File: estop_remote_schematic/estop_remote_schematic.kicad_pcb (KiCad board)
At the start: 2 copper layers, 13 parts

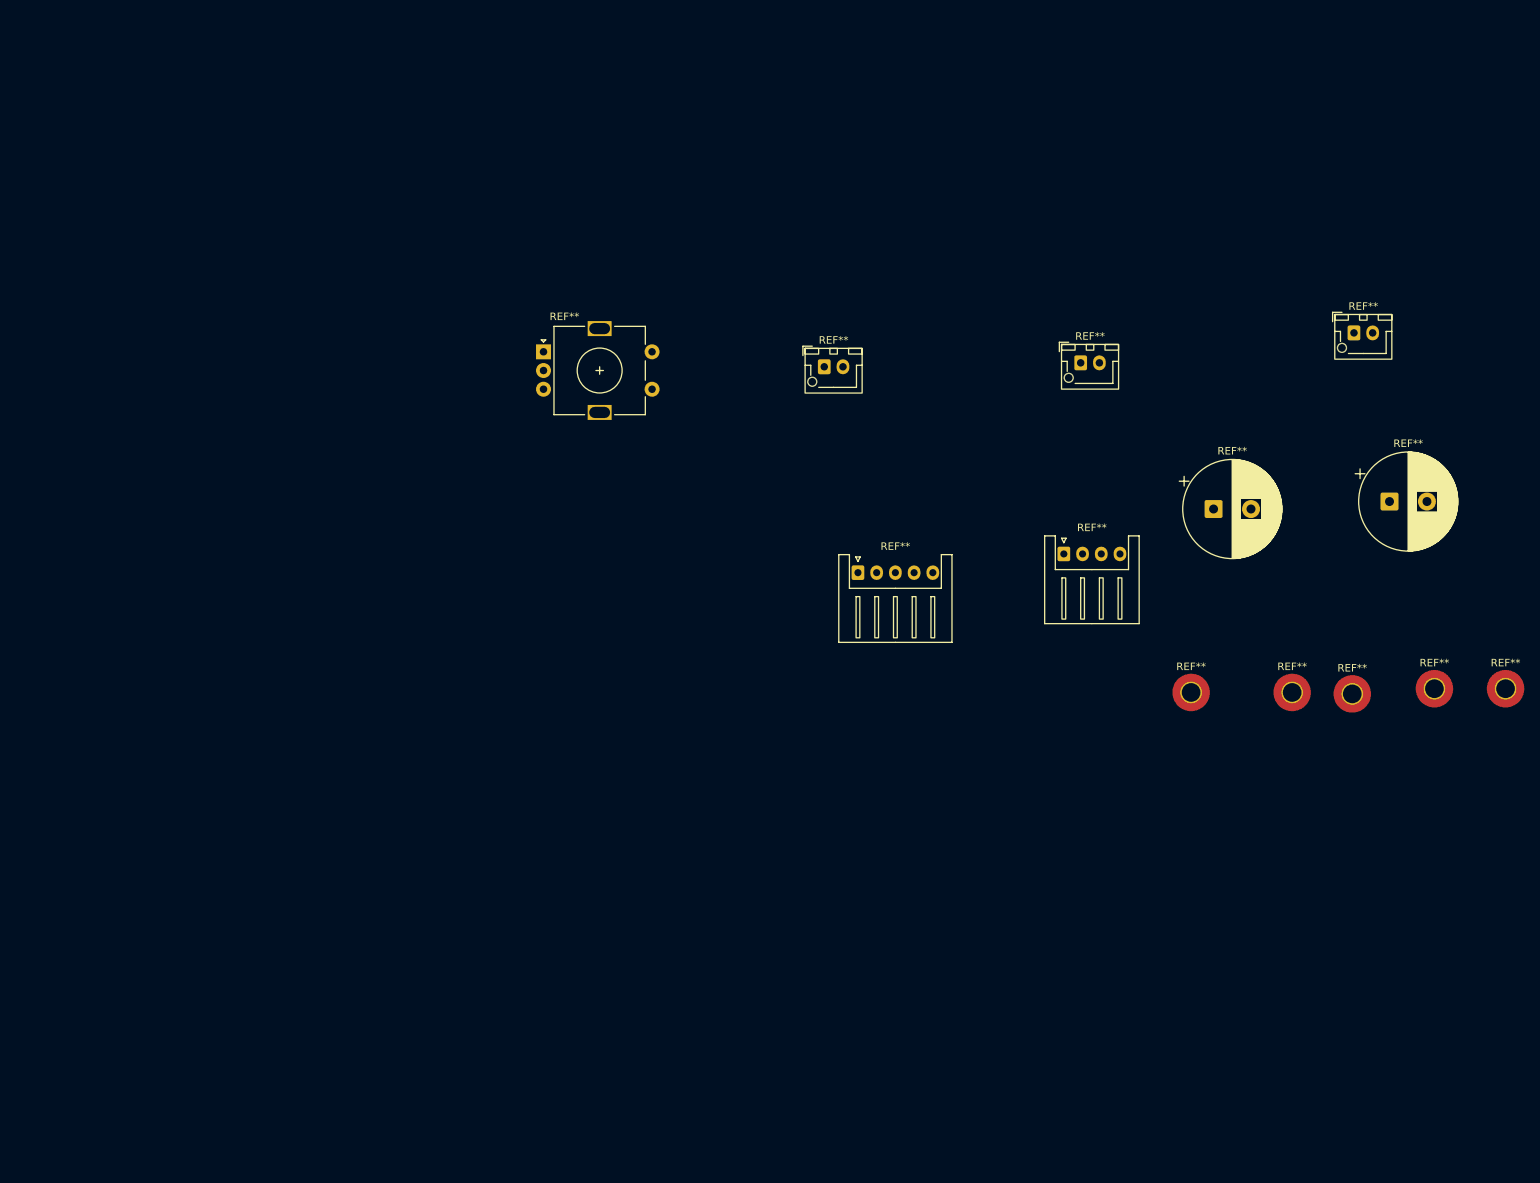
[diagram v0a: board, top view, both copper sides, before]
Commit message: updated footprints, cleaned up global labels and updated preliminary PCB to be more accurate
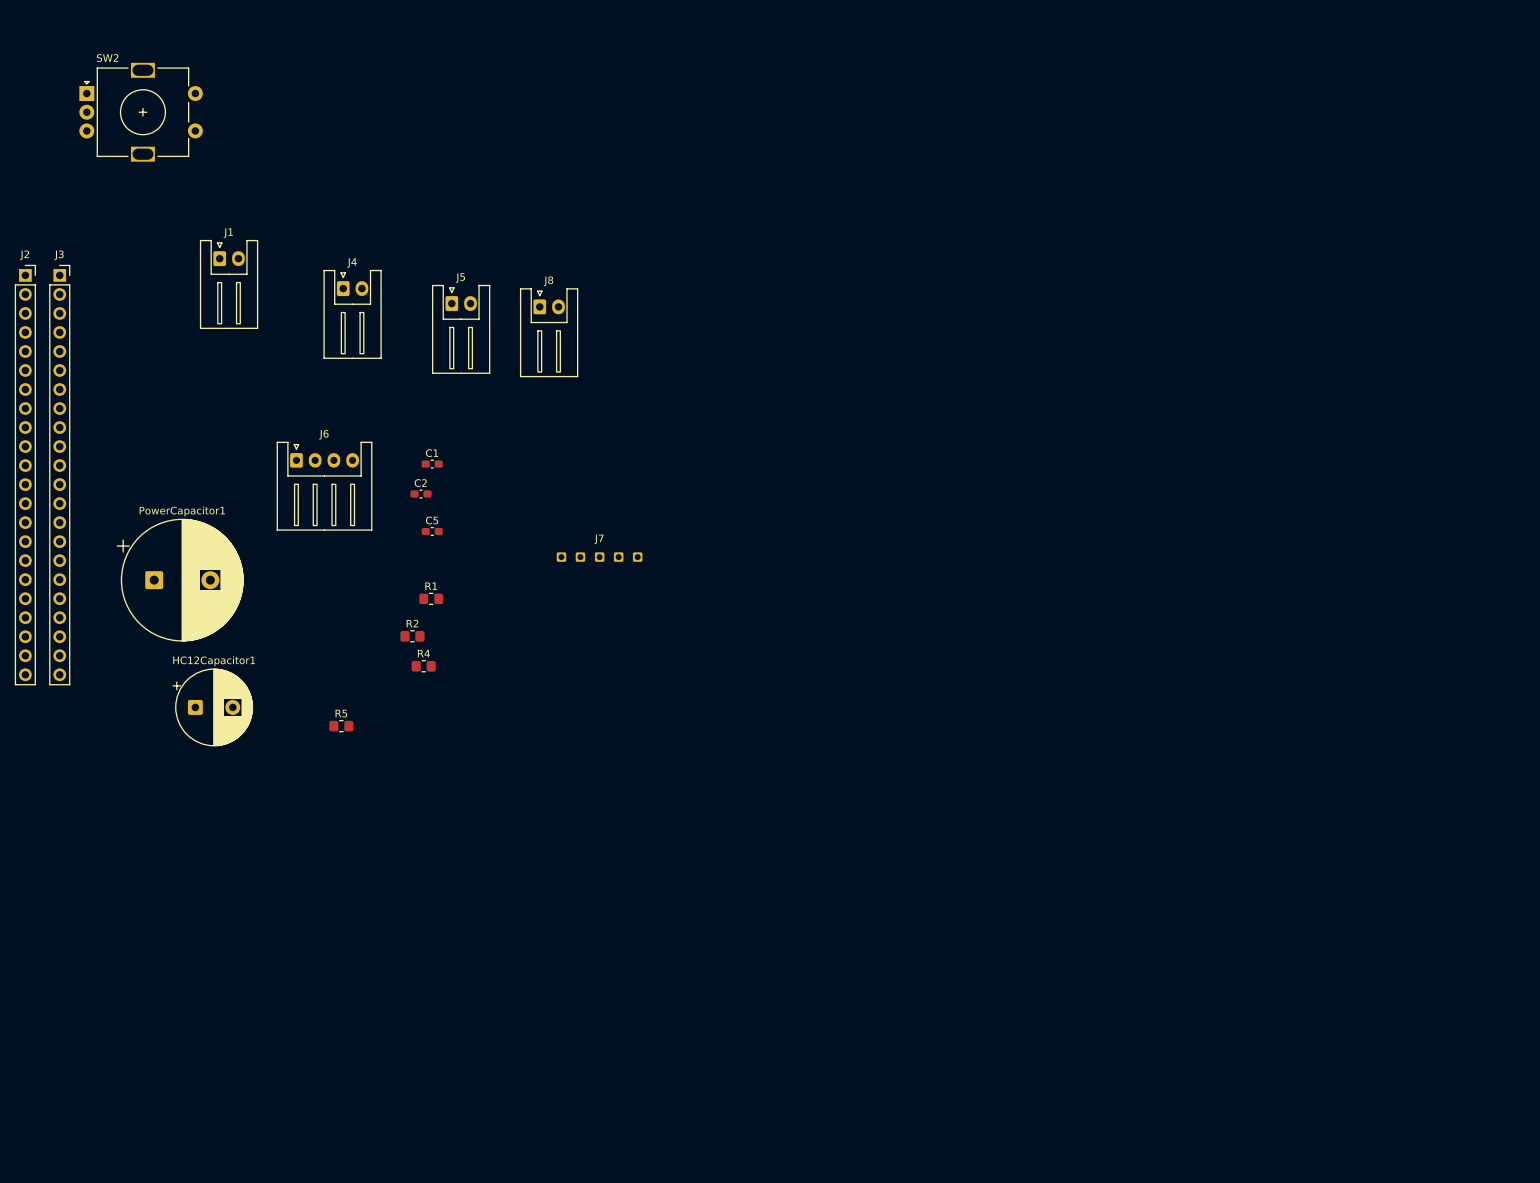
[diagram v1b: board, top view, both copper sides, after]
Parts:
- removed REF**: JST_XH_S5B-XH-A_1x05_P2.50mm_Horizontal, Connector_JST:JST_XH_S5B-XH-A_1x05_P2.50mm_Horizontal
- removed REF**: JST_XH_S4B-XH-A_1x04_P2.50mm_Horizontal, Connector_JST:JST_XH_S4B-XH-A_1x04_P2.50mm_Horizontal
- removed REF** (x3): JST_XH_B2B-XH-AM_1x02_P2.50mm_Vertical, Connector_JST:JST_XH_B2B-XH-AM_1x02_P2.50mm_Vertical
- removed REF** (x5): MountingHole_2.5mm_Pad_TopOnly, MountingHole:MountingHole_2.5mm_Pad_TopOnly
- removed REF**: RotaryEncoder_Alps_EC11E-Switch_Vertical_H20mm, Rotary_Encoder:RotaryEncoder_Alps_EC11E-Switch_Vertical_H20mm
- removed REF** (x2): CP_Radial_D13.0mm_P5.00mm, Capacitor_THT:CP_Radial_D13.0mm_P5.00mm
- added C1: 0.1uF, Capacitor_SMD:C_0603_1608Metric_Pad1.08x0.95mm_HandSolder, F.Cu at (113.1, 88.0)
- added C2: 0.1uF, Capacitor_SMD:C_0603_1608Metric_Pad1.08x0.95mm_HandSolder, F.Cu at (111.6, 92.0)
- added C5: 0.1uF, Capacitor_SMD:C_0603_1608Metric_Pad1.08x0.95mm_HandSolder, F.Cu at (113.1, 97.0)
- added HC12Capacitor1: 220uF, Capacitor_THT:CP_Radial_D10.0mm_P5.00mm, F.Cu at (81.5, 120.5)
- added J1: Power Switch, Connector_JST:JST_XH_S2B-XH-A_1x02_P2.50mm_Horizontal, F.Cu at (84.8, 60.6)
- added J2: ESP32 Pins 1-22, Connector_PinSocket_2.54mm:PinSocket_1x22_P2.54mm_Vertical, F.Cu at (58.8, 62.8)
- added J3: ESP32 Pins 23-44, Connector_PinSocket_2.54mm:PinSocket_1x22_P2.54mm_Vertical, F.Cu at (63.4, 62.8)
- added J4: Battery Connector, Connector_JST:JST_XH_S2B-XH-A_1x02_P2.50mm_Horizontal, F.Cu at (101.2, 64.6)
- added J5: EStop Button, Connector_JST:JST_XH_S2B-XH-A_1x02_P2.50mm_Horizontal, F.Cu at (115.8, 66.6)
- added J6: OLed Screen Pins, Connector_JST:JST_XH_S4B-XH-A_1x04_P2.50mm_Horizontal, F.Cu at (95.0, 87.5)
- added J7: HC12 Connections, holes:2.54mm-5-holes, F.Cu at (135.5, 100.5)
- added J8: Reset Button, Connector_JST:JST_XH_S2B-XH-A_1x02_P2.50mm_Horizontal, F.Cu at (127.5, 67.0)
- added PowerCapacitor1: 2200uF, Capacitor_THT:CP_Radial_D16.0mm_P7.50mm, F.Cu at (76.0, 103.5)
- added R1: 47kΩ, Resistor_SMD:R_0805_2012Metric_Pad1.20x1.40mm_HandSolder, F.Cu at (113.0, 106.0)
- added R2: 10kΩ, Resistor_SMD:R_0805_2012Metric_Pad1.20x1.40mm_HandSolder, F.Cu at (110.5, 111.0)
- added R4: 4.7kΩ, Resistor_SMD:R_0805_2012Metric_Pad1.20x1.40mm_HandSolder, F.Cu at (112.0, 115.0)
- added R5: 4.7kΩ, Resistor_SMD:R_0805_2012Metric_Pad1.20x1.40mm_HandSolder, F.Cu at (101.0, 123.0)
- added SW2: RotaryEncoder_Switch_MP, Rotary_Encoder:RotaryEncoder_Alps_EC11E-Switch_Vertical_H20mm, F.Cu at (67.0, 38.5)

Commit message: added initial PCB cut edges
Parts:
- added REF**: MountingHole_2.2mm_M2, MountingHole:MountingHole_2.2mm_M2, F.Cu at (82.0, 178.0)
- added REF**: MountingHole_2.2mm_M2, MountingHole:MountingHole_2.2mm_M2, F.Cu at (124.0, 178.0)
- added REF**: MountingHole_2.2mm_M2, MountingHole:MountingHole_2.2mm_M2, F.Cu at (81.5, 35.5)
- added REF**: MountingHole_2.2mm_M2, MountingHole:MountingHole_2.2mm_M2, F.Cu at (124.5, 35.5)
- HC12Capacitor1: footprint Capacitor_THT:CP_Radial_D10.0mm_P5.00mm -> Capacitor_THT:CP_Radial_D7.5mm_P2.50mm
- J1: footprint Connector_JST:JST_XH_S2B-XH-A_1x02_P2.50mm_Horizontal -> Connector_JST:JST_XH_B2B-XH-AM_1x02_P2.50mm_Vertical
- J4, J5, J8: footprint Connector_JST:JST_XH_S2B-XH-A_1x02_P2.50mm_Horizontal -> Connector_JST:JST_XH_B2B-XH-A_1x02_P2.50mm_Vertical
- J6: footprint Connector_JST:JST_XH_S4B-XH-A_1x04_P2.50mm_Horizontal -> Connector_JST:JST_XH_S4B-XH-A-1_1x04_P2.50mm_Horizontal
- J7: footprint holes:2.54mm-5-holes -> Connector_PinHeader_2.54mm:PinHeader_1x05_P2.54mm_Vertical
- PowerCapacitor1: footprint Capacitor_THT:CP_Radial_D16.0mm_P7.50mm -> Capacitor_THT:CP_Radial_D10.0mm_P5.00mm
- moved SW2 135.3 mm to (96.5, 170.5)
- moved J1 67.0 mm to (120.0, 117.5)
- moved J7 64.5 mm to (80.3, 67.0), turned to 90 degrees
- moved J8 62.9 mm to (120.5, 129.5)
- moved J3 61.1 mm to (119.5, 38.7)
- moved J6 56.1 mm to (82.2, 142.2)
- moved I2CPullup1 53.4 mm to (153.0, 111.0)
- moved J2 46.1 mm to (94.5, 92.0), turned to 180 degrees
- moved HC12Capacitor1 44.0 mm to (82.5, 76.5)
- moved J5 43.1 mm to (95.2, 104.5)
- moved PowerCapacitor1 42.5 mm to (118.5, 105.0)
- moved J4 40.5 mm to (108.0, 104.5)
- moved HC12DecouplingCapacitor1 37.4 mm to (81.4, 70.0)
- moved I2CPullup2 30.0 mm to (142.0, 115.5)
- moved VoltDivResistor2 27.6 mm to (112.5, 83.5), turned to 90 degrees
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- renumbered C5 to ADCDecouplingCapacitor1, C2 to HC12DecouplingCapacitor1, R5 to I2CPullup1, R4 to I2CPullup2, C1 to PowerCapacitor2, R1 to VoltDivResistor1, R2 to VoltDivResistor2
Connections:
- J1 pad 1: +6V -> Net-(J1-Pin_1)
- J1 pad 2: Net-(J1-Pin_2) -> +6V
- J2 pad 21: unconnected-(J2-Pin_21-Pad21) -> +6V
- J4 pad 1: Net-(J1-Pin_2) -> Net-(J1-Pin_1)
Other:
- board outline added: 50 x 150 mm

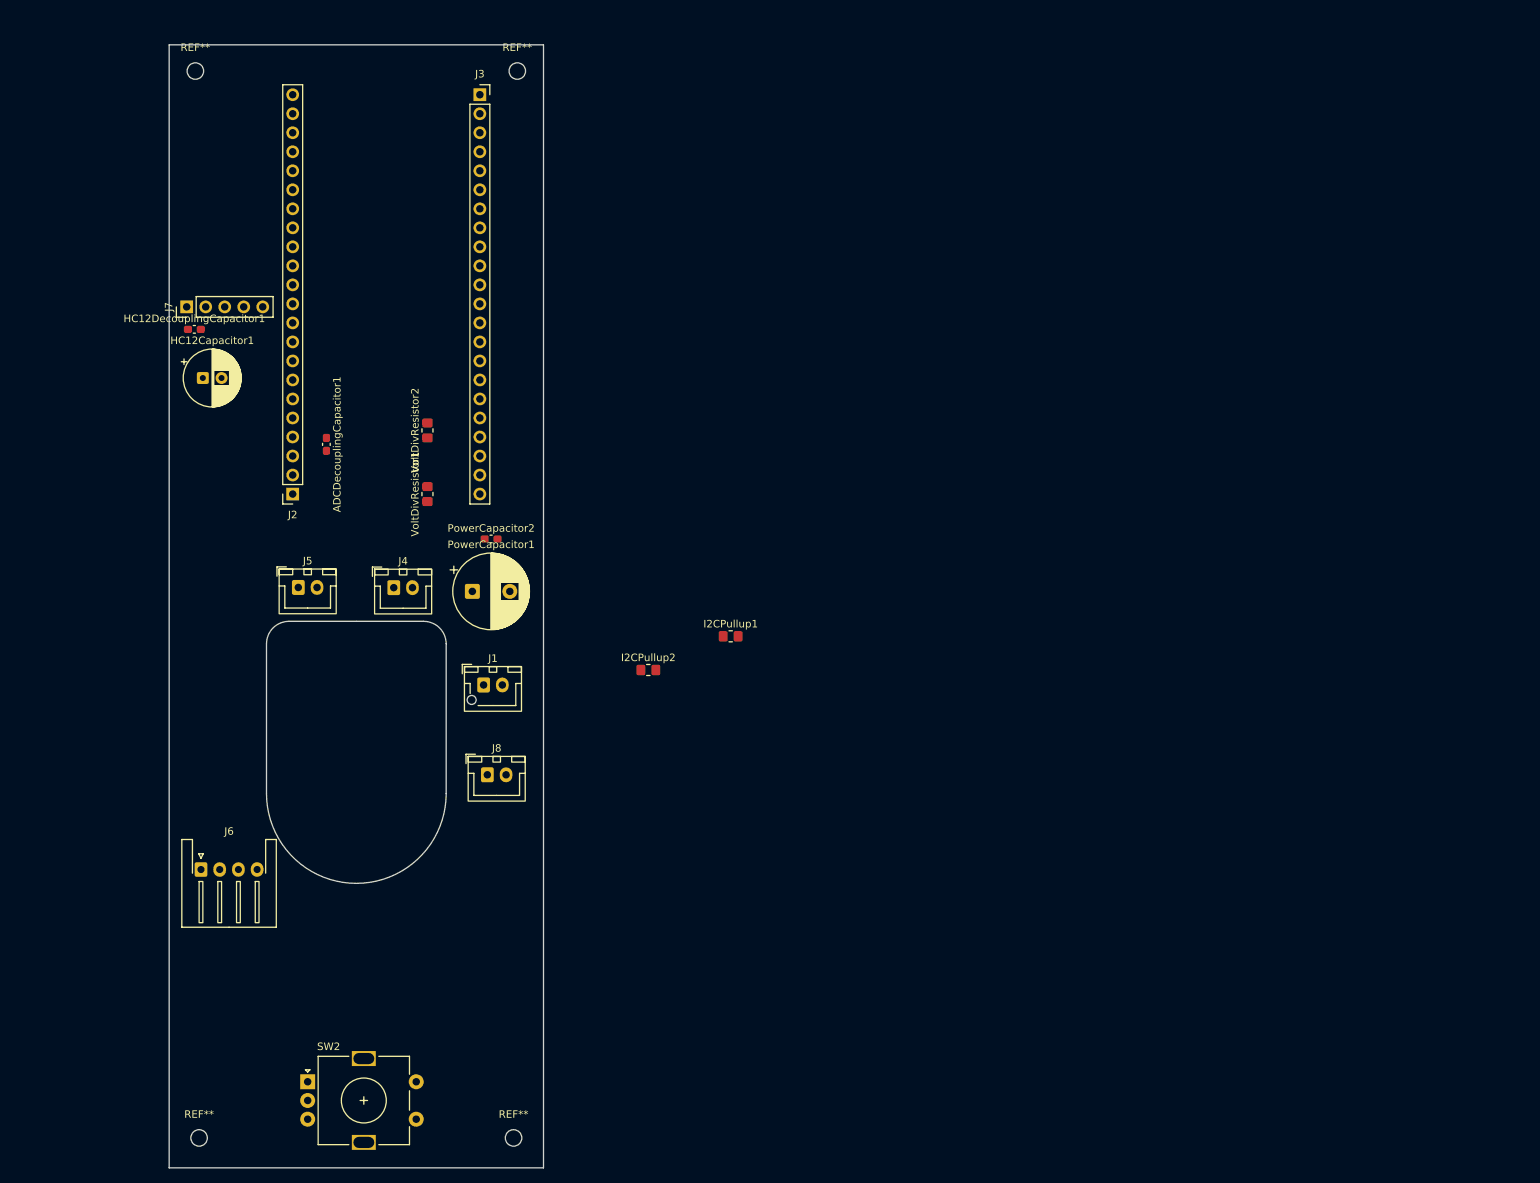
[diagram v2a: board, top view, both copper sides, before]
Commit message: Adjusted layout of PCB to shrink size and optimize trace layout
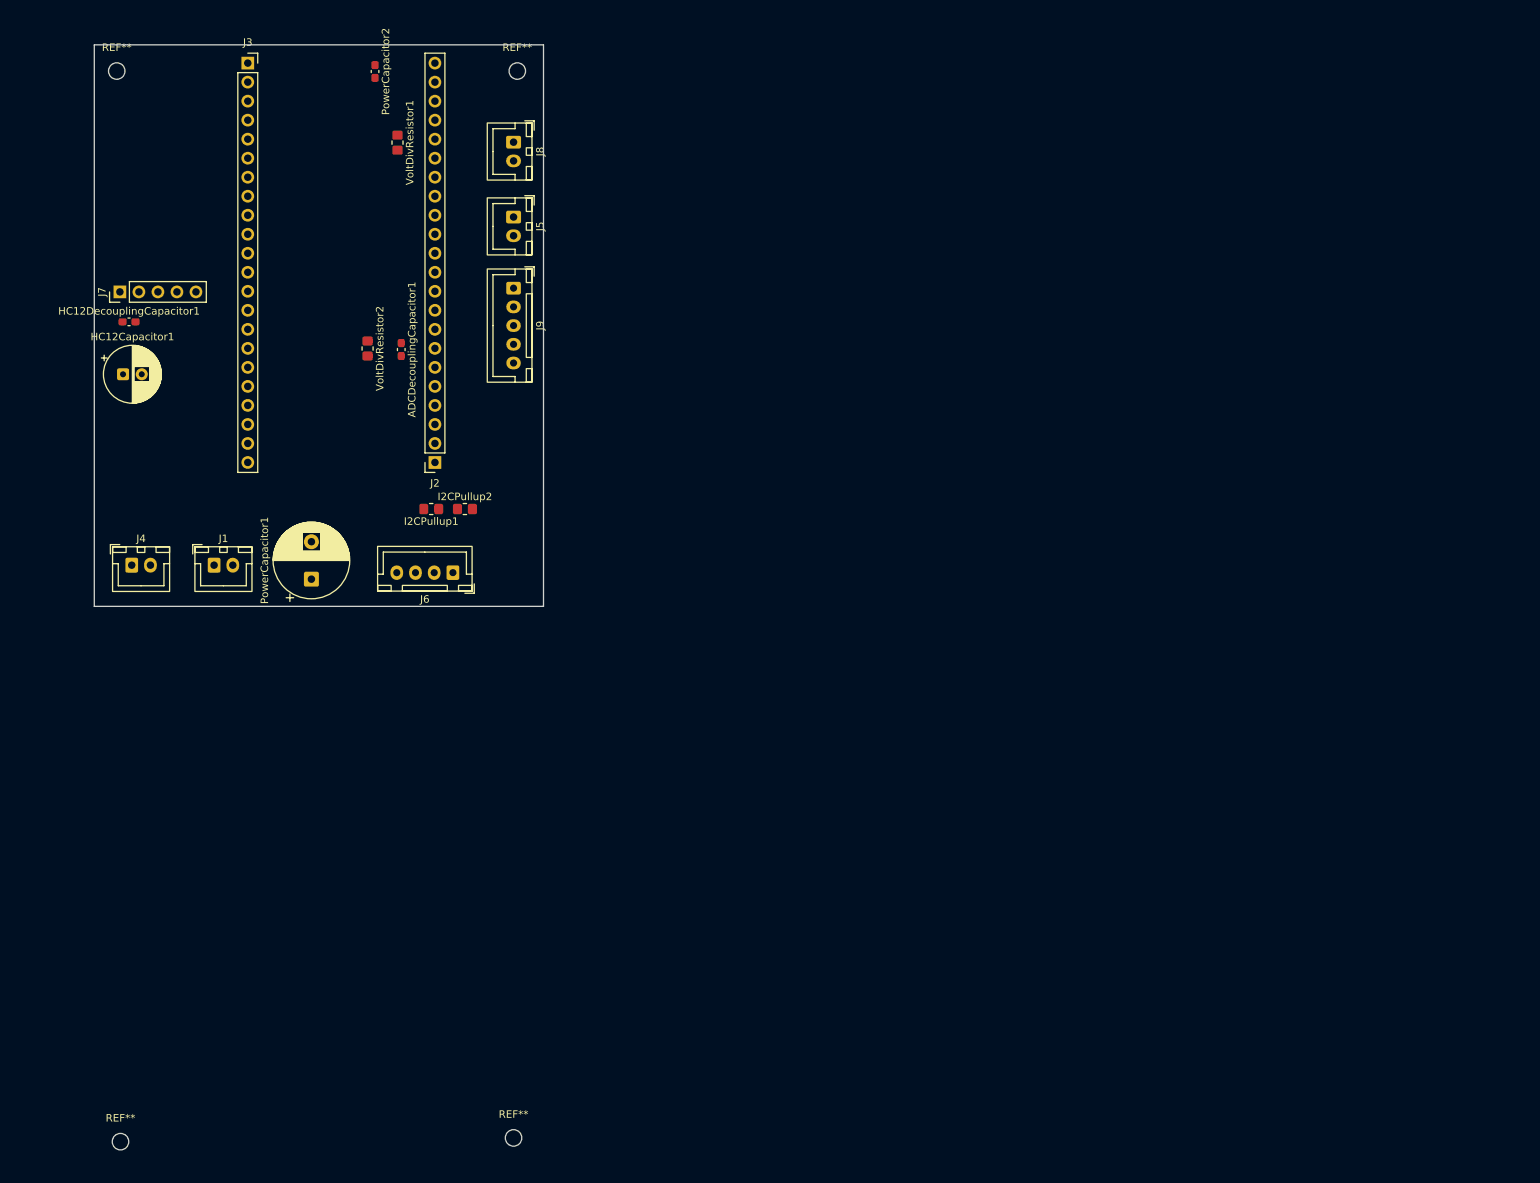
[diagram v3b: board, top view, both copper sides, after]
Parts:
- removed SW2: RotaryEncoder_Switch_MP, Rotary_Encoder:RotaryEncoder_Alps_EC11E-Switch_Vertical_H20mm
- added J9: RotaryEnc Connections, Connector_JST:JST_XH_B5B-XH-A_1x05_P2.50mm_Vertical, F.Cu at (124.0, 64.5)
- J1: footprint Connector_JST:JST_XH_B2B-XH-AM_1x02_P2.50mm_Vertical -> Connector_JST:JST_XH_B2B-XH-A_1x02_P2.50mm_Vertical
- J6: footprint Connector_JST:JST_XH_S4B-XH-A-1_1x04_P2.50mm_Horizontal -> Connector_JST:JST_XH_B4B-XH-A_1x04_P2.50mm_Vertical
- moved J8 84.6 mm to (124.0, 45.0), turned to -90 degrees
- moved PowerCapacitor2 64.3 mm to (105.5, 35.6), turned to -90 degrees
- moved J5 57.2 mm to (124.0, 55.0), turned to -90 degrees
- moved J6 52.0 mm to (115.9, 102.5), turned to 180 degrees
- moved VoltDivResistor1 47.1 mm to (108.5, 45.1), turned to -90 degrees
- moved I2CPullup1 43.5 mm to (113.0, 94.0), turned to 180 degrees
- moved J1 39.4 mm to (84.0, 101.5)
- moved J4 35.1 mm to (73.0, 101.5)
- moved I2CPullup2 32.6 mm to (117.5, 94.0)
- moved J3 31.3 mm to (88.5, 34.4)
- moved PowerCapacitor1 21.6 mm to (97.0, 103.4), turned to 90 degrees
- moved J2 19.5 mm to (113.5, 87.8)
- moved ADCDecouplingCapacitor1 16.1 mm to (109.0, 72.7)
- moved VoltDivResistor2 13.6 mm to (104.5, 72.6), turned to -90 degrees
- moved HC12Capacitor1 10.7 mm to (71.8, 76.0)
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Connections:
- J2 pad 10: /HC12_RX -> /ChannelEncoderSignal
- J2 pad 11: /HC12_TX -> /ChannelEncoderA
- J2 pad 12: unconnected-(J2-Pin_12-Pad12) -> /ChannelEncoderB
- J2 pad 4: /BatteryVoltageDivider -> unconnected-(J2-Pin_4-Pad4)
- J2 pad 5: /HC12_SET -> unconnected-(J2-Pin_5-Pad5)
- J2 pad 6: /ChannelEncoderSignal -> /SCL
- J2 pad 7: /EStopSignal -> /SDA
- J2 pad 8: /ChannelEncoderA -> /EStopSignal
- J2 pad 9: /ChannelEncoderB -> /BatteryVoltageDivider
- J3 pad 18: /SCL -> /HC12_TX
- J3 pad 19: /SDA -> /HC12_RX
- J3 pad 5: unconnected-(J3-Pin_5-Pad5) -> /HC12_SET
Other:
- board size 50 x 150 mm -> 60 x 75 mm
